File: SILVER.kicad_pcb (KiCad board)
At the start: 2 copper layers, 120 x 80 mm, 53 parts, among them J1 Conn_01x13, J10 Conn_02x22_Odd_Even_MountingP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, J11 UltraRight, J2 UltraLeft, J3 MPU6050, J4 MotorL, J5 MotorR, J6 XT60-M, J7 STLINK, J8 Conn_01x04_Pin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

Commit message: pcbv1.0
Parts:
- removed C1, C5: 33nF, Capacitor_SMD:C_0805_2012Metric
- removed C12, C15, C2, C4, C6, C8: 0.1u, Capacitor_SMD:C_0805_2012Metric
- removed C13, C14, C16, C17: NP, Capacitor_SMD:C_Elec_6.3x5.4
- removed C18, C19: 330u, Capacitor_SMD:CP_Elec_8x10.5
- removed C3, C7: 47uF, Capacitor_SMD:C_Elec_6.3x5.4
- removed D3, D6: GREEN, LED_SMD:LED_0603_1608Metric
- removed D4, D5: RED, LED_SMD:LED_0603_1608Metric
- removed D7: SS34, Diode_SMD:D_SMA
- removed L2: 47uH, Inductor_SMD:L_12x12mm_H6mm
- removed Q1, Q2: FCD600N60Z, Package_TO_SOT_SMD:TO-252-2
- removed R1, R10, R18, R9: 10k, Resistor_SMD:R_0508_1220Metric
- removed R11, R12, R15, R16, R2, R3, R6, R7: 1k, Resistor_SMD:R_0508_1220Metric
- removed R24, R25: 4.7k, Resistor_SMD:R_0508_1220Metric
- removed U1, U2: VNH5019A-E, Package_SO:ST_MultiPowerSO-30
- removed U4: LM2596S-5.0, Package_TO_SOT_SMD:TO-263-5_TabPin3
- added D1: LED_RGBK, Connector_PinSocket_2.54mm:PinSocket_2x02_P2.54mm_Vertical, F.Cu at (242.5, 112.5)
- added J12: Conn_01x02_Pin, Connector_PinHeader_2.54mm:PinHeader_1x02_P2.54mm_Vertical, F.Cu at (242.5, 121.5)
- added J14: Screw_Terminal_01x02, TerminalBlock:TerminalBlock_MaiXu_MX126-5.0-02P_1x02_P5.00mm, F.Cu at (227.8, 91.0)
- added J15: Screw_Terminal_01x02, TerminalBlock:TerminalBlock_MaiXu_MX126-5.0-02P_1x02_P5.00mm, F.Cu at (247.0, 130.0)
- added J16: Screw_Terminal_01x02, TerminalBlock:TerminalBlock_MaiXu_MX126-5.0-02P_1x02_P5.00mm, F.Cu at (162.5, 130.5)
- added J17: Screw_Terminal_01x02, TerminalBlock:TerminalBlock_MaiXu_MX126-5.0-02P_1x02_P5.00mm, F.Cu at (165.5, 116.2)
- added J18: Conn_01x02_Pin, Connector_PinHeader_2.54mm:PinHeader_1x02_P2.54mm_Vertical, F.Cu at (153.7, 122.0)
- J1: footprint Connector_FFC-FPC:Hirose_FH12-13S-0.5SH_1x13-1MP_P0.50mm_Horizontal -> Connector_PinHeader_2.54mm:PinHeader_1x13_P2.54mm_Vertical
- SW1: footprint Library:SW_RB141C1100 -> Library:KCD11-101
- moved J6 201.8 mm to (232.0, 124.6), turned to 90 degrees
- moved J8 201.7 mm to (231.5, 141.0), turned to 180 degrees
- moved J7 189.4 mm to (201.4, 139.8), turned to 180 degrees
- moved J11 187.4 mm to (228.0, 76.0)
- moved SW1 173.6 mm to (231.5, 104.0), turned to -90 degrees
- moved J5 163.7 mm to (250.6, 137.5), turned to -90 degrees
- moved J2 140.7 mm to (172.0, 76.0)
- moved J3 124.9 mm to (173.5, 109.8), turned to 180 degrees
- moved J1 118.9 mm to (184.8, 72.5), turned to 90 degrees
- moved J4 87.9 mm to (162.3, 138.0), turned to -90 degrees
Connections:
- J11 pad 2: E6 -> B8
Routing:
- net +3.3V: track 0.00 -> 200.8 mm
- net +5V: track 0.00 -> 132.8 mm
- net B4: track 0.00 -> 91.8 mm, vias 0 -> 2
- net B5: track 0.00 -> 90.3 mm, vias 0 -> 3
- net B0: track 0.00 -> 70.0 mm, vias 0 -> 1
- net D13: track 0.00 -> 68.5 mm, vias 0 -> 1
- net E4: track 0.00 -> 68.4 mm
- net NR: track 0.00 -> 68.1 mm
- net E9: track 0.00 -> 66.9 mm, vias 0 -> 1
- net D12: track 0.00 -> 66.1 mm
- net E7: track 0.00 -> 65.6 mm, vias 0 -> 1
- net E8: track 0.00 -> 64.3 mm, vias 0 -> 1
- net B1: track 0.00 -> 63.5 mm, vias 0 -> 4
- net C5: track 0.00 -> 61.5 mm, vias 0 -> 3
- net C4: track 0.00 -> 60.7 mm, vias 0 -> 3
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- added copper zone on F.Cu, net +12V
- added copper zone on B.Cu, net GND
- added copper zone on F.Cu, net GND
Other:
- outline, holes or cut-outs redrawn

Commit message: SILVER PCB v2.0
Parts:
- removed D1: LED_RGBK, Connector_PinSocket_2.54mm:PinSocket_2x02_P2.54mm_Vertical
- added D2: APFA3010, Connector_PinSocket_2.54mm:PinSocket_2x02_P2.54mm_Vertical, F.Cu at (243.3, 113.2)
- added R1: R, Resistor_THT:R_Axial_DIN0204_L3.6mm_D1.6mm_P2.54mm_Vertical, F.Cu at (240.5, 107.3)
- J1: footprint Connector_PinHeader_2.54mm:PinHeader_1x13_P2.54mm_Vertical -> Connector_PinHeader_2.54mm:PinHeader_1x13_P2.54mm_Vertical_SMD_Pin1Left
- moved J1 15.4 mm to (200.0, 75.0)
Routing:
- net E7: track 65.6 -> 115.6 mm, vias 1 -> 3
- net NR: track 68.1 -> 117.1 mm, vias 0 -> 1
- net B1: track 63.5 -> 104.9 mm, vias 4 -> 3
- net +5V: track 132.8 -> 172.1 mm
- net E9: track 66.9 -> 104.4 mm, vias 1 -> 5
- net B5: track 90.3 -> 126.1 mm, vias 3 -> 1
- net B7: track 55.7 -> 82.9 mm, vias 1 -> 2
- net D14: track 29.9 -> 51.8 mm, vias 0 -> 2
- net C6: track 27.2 -> 49.0 mm, vias 0 -> 1
- net A7: track 52.6 -> 73.9 mm
- net D13: track 68.5 -> 89.7 mm, vias 1 -> 2
- net E8: track 64.3 -> 83.2 mm, vias 1 -> 4
- net D12: track 66.1 -> 82.0 mm
- net B6: track 56.8 -> 70.5 mm, vias 0 -> 1
- net B0: track 70.0 -> 58.3 mm, vias 1 -> 2
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- removed copper zone on F.Cu, net +12V
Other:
- outline, holes or cut-outs redrawn

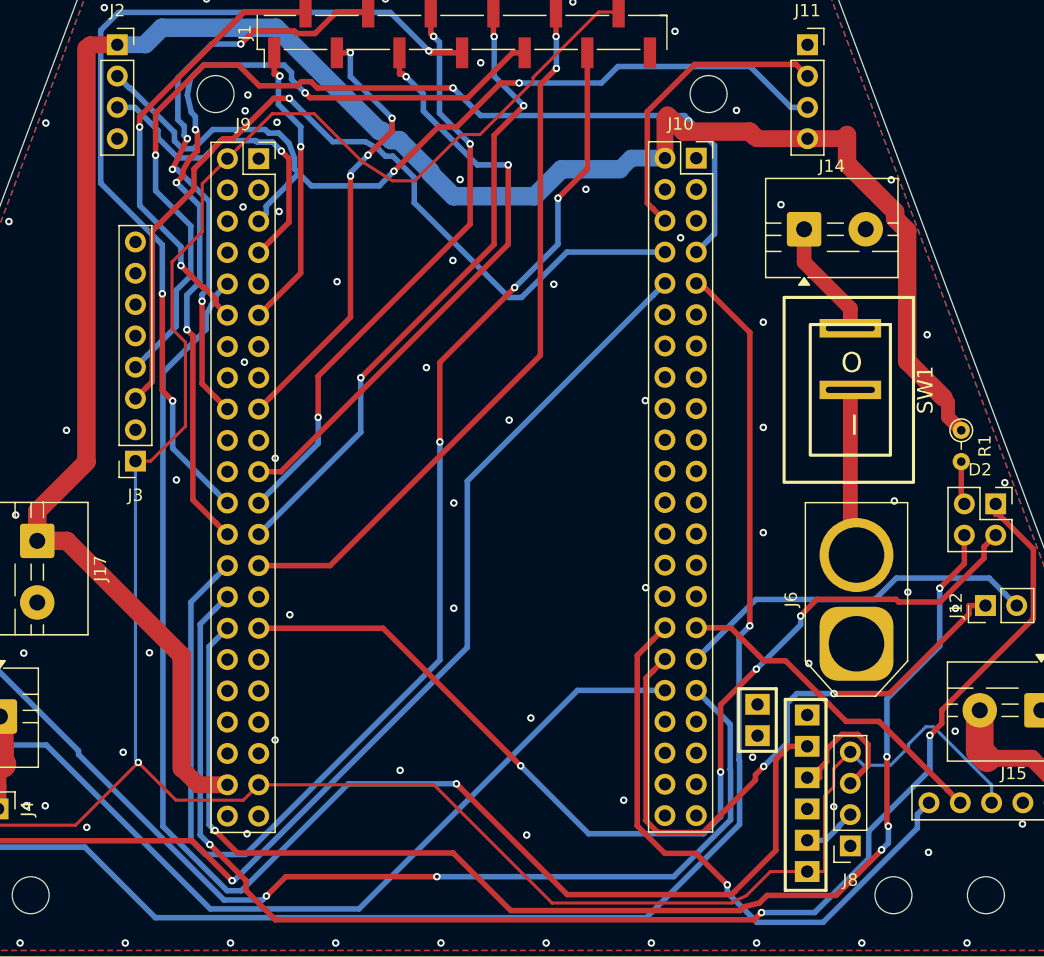
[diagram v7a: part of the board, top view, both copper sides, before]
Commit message: Cleaned up the middle traces and right edge 5v trace
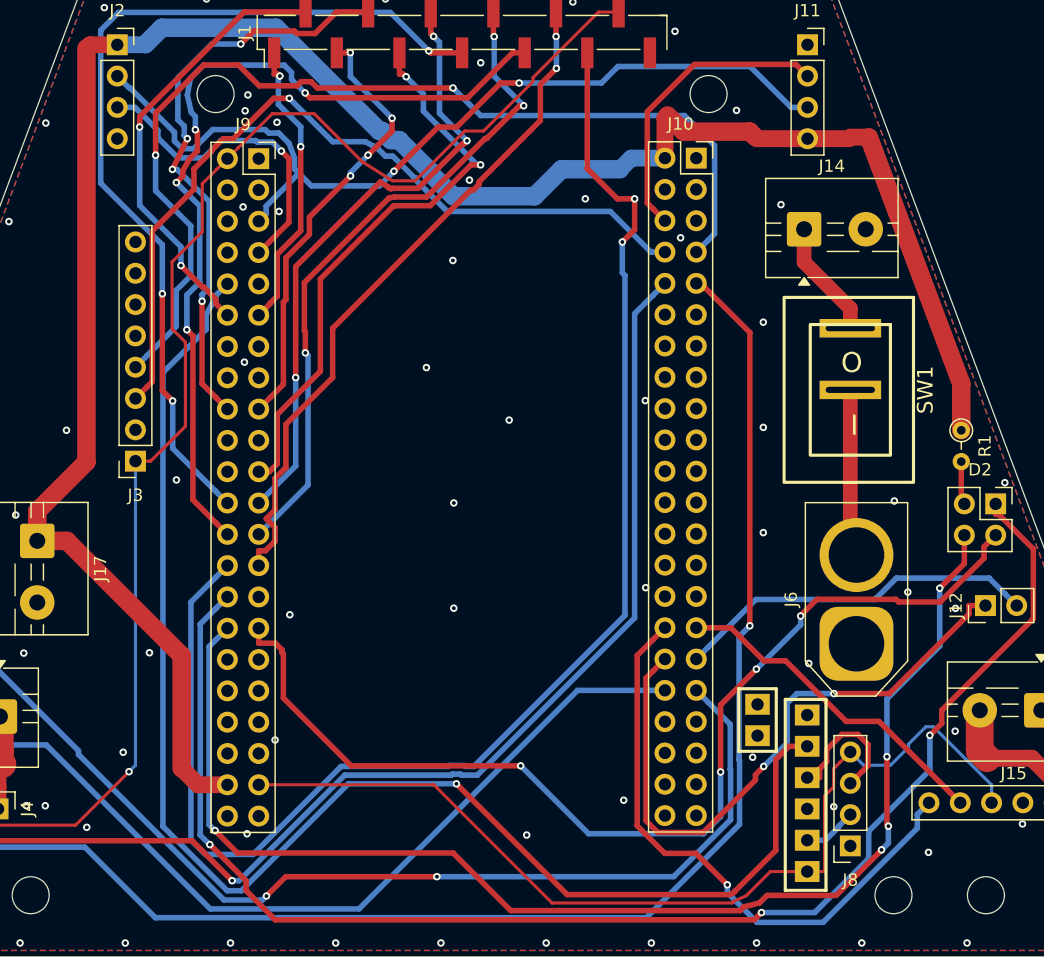
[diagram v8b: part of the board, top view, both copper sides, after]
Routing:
- net +5V: track 172.1 -> 149.7 mm
- net +3.3V: track 206.3 -> 194.6 mm
- net B1: track 104.9 -> 115.8 mm, vias 3 -> 2
- net B4: track 94.7 -> 101.3 mm
- net B6: track 70.5 -> 66.4 mm
- net E8: track 83.2 -> 86.1 mm
- net B0: track 58.3 -> 56.0 mm
- net A6: track 48.3 -> 50.6 mm
- net C4: track 52.3 -> 54.5 mm
- net A4: track 48.7 -> 47.2 mm
- net GND: vias 84 -> 77
